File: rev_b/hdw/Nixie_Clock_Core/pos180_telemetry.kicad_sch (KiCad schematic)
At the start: 27 parts, among them Q701 BSS192PH6327FTSA1, U701 OPA333xxDCK, U704 OPA333xxDCK, U705 OPA333xxDCK

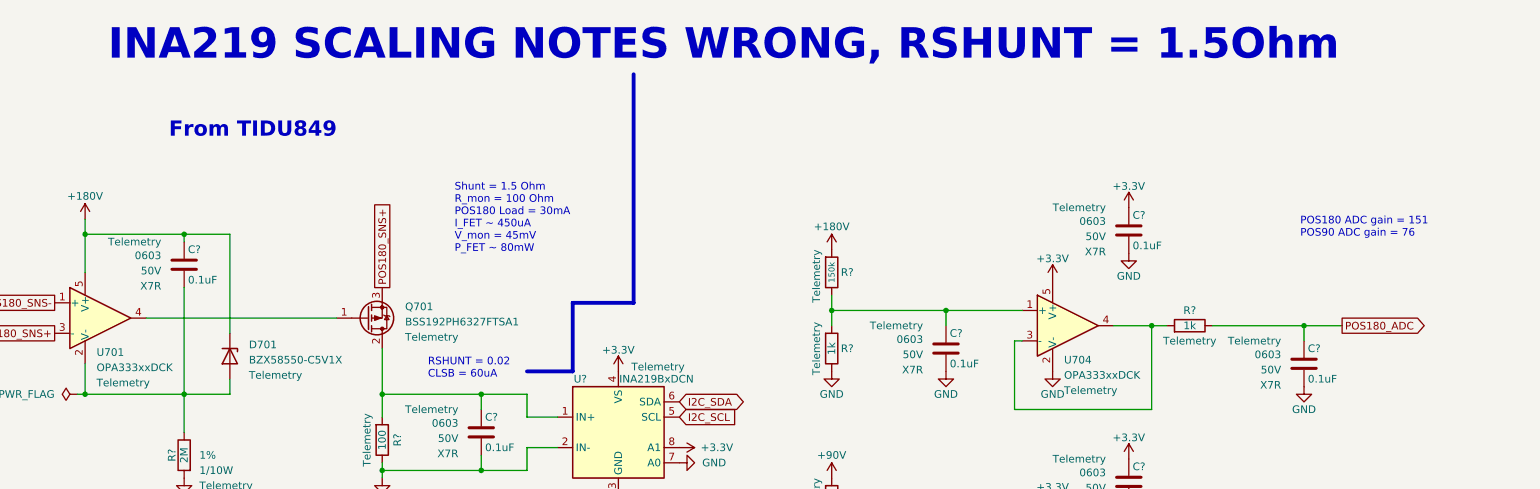
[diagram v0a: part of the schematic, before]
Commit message: added BOM
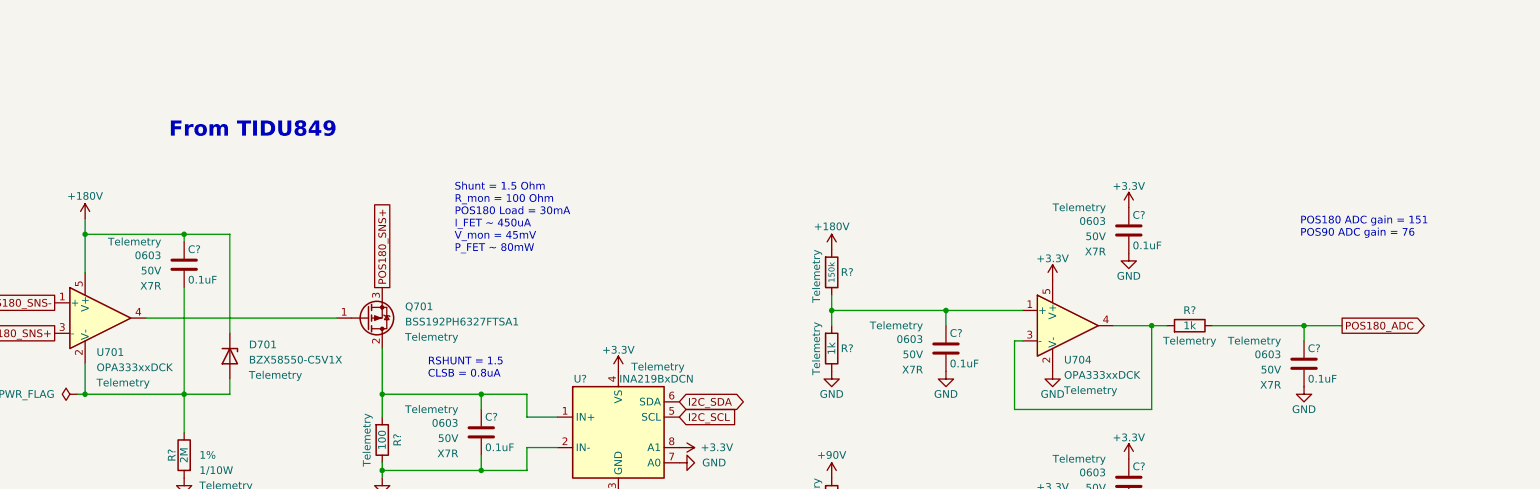
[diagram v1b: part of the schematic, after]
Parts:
- R?: Digi-Key PN (none) -> 541-CRCW0603150KFKTACT-ND
- R? (x4): Digi-Key PN (none) -> 541-1.00KHCT-ND
- R?: Digi-Key PN (none) -> 541-5552-1-ND
- R?: Digi-Key PN (none) -> 541-3951-1-ND
- R?: Digi-Key PN (none) -> 541-5333-1-ND
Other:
- note added: "RSHUNT = 1.5 CLSB = 0.8uA"
- note removed: "INA219 SCALING NOTES WRONG, RSHUNT = 1.5Ohm"
- note removed: "RSHUNT = 0.02 CLSB = 60uA"
- title: (none) -> Nixie Clock Redux Core Board
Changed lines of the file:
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@@
   (paper "A")
   (title_block
-    (date "2023-05-12")
-    (rev "PRELIM")
+    (title "Nixie Clock Redux Core Board")
+    (date "2023-07-30")
+    (rev "B")
     (company "Drew Maatman")
   )
@@
     (stroke (width 0) (type default))
   )
-  (polyline (pts (xy 128.27 34.29) (xy 128.27 72.39))
-    (stroke (width 0.635) (type default) (color 255 0 0 1))
-  )
   (wire (pts (xy 208.28 114.3) (xy 214.63 114.3))
     (stroke (width 0) (type default))
@@
     (stroke (width 0) (type default))
   )
-  (polyline (pts (xy 118.11 72.39) (xy 128.27 72.39))
-    (stroke (width 0.635) (type default) (color 255 0 0 1))
-  )
   (wire (pts (xy 86.36 100.33) (xy 86.36 101.6))
     (stroke (width 0) (type default))
@@
     (stroke (width 0) (type default))
   )
-  (polyline (pts (xy 110.49 83.82) (xy 118.11 83.82))
-    (stroke (width 0.635) (type default) (color 255 0 0 1))
-  )
   (wire (pts (xy 86.36 100.33) (xy 102.87 100.33))
     (stroke (width 0) (type default))
@@
     (stroke (width 0) (type default))
   )
-  (polyline (pts (xy 118.11 83.82) (xy 118.11 72.39))
-    (stroke (width 0.635) (type default) (color 255 0 0 1))
-  )
   (wire (pts (xy 224.79 76.2) (xy 240.03 76.2))
     (stroke (width 0) (type default))
@@
     (effects (font (size 1.27 1.27)) (justify left bottom))
   )
-  (text "RSHUNT = 0.02\nCLSB = 60uA" (at 93.98 85.09 0)
+  (text "RSHUNT = 1.5\nCLSB = 0.8uA" (at 93.98 85.09 0)
     (effects (font (size 1.27 1.27)) (justify left bottom))
   )
@@
     (effects (font (size 1.27 1.27)) (justify left bottom))
   )
-  (text "INA219 SCALING NOTES WRONG, RSHUNT = 1.5Ohm" (at 40.64 32.385 0)
-    (effects (font (face "Courier New") (size 5.08 5.08) (thickness 0.254) bold (color 255 37 56 1)) (justify left bottom))
-  )
-  (global_label "I2C_SDA" (shape bidirectional) (at 135.89 88.9 0)
+  (global_label "I2C_SDA" (shape bidirectional) (at 135.89 88.9 0) (fields_autoplaced)
     (effects (font (size 1.27 1.27)) (justify left))
-    (property "Intersheetrefs" "${INTERSHEET_REFS}" (at 135.89 88.9 0)
-      (effects (font (size 1.27 1.27)) hide)
+    (property "Intersheetrefs" "${INTERSHEET_REFS}" (at 147.5271 88.9 0)
+      (effects (font (size 1.27 1.27)) (justify left))
     )
   )
-  (global_label "I2C_SDA" (shape bidirectional) (at 57.15 156.21 0)
+  (global_label "I2C_SDA" (shape bidirectional) (at 57.15 156.21 0) (fields_autoplaced)
     (effects (font (size 1.27 1.27)) (justify left))
-    (property "Intersheetrefs" "${INTERSHEET_REFS}" (at 57.15 156.21 0)
-      (effects (font (size 1.27 1.27)) hide)
+    (property "Intersheetrefs" "${INTERSHEET_REFS}" (at 68.7871 156.21 0)
+      (effects (font (size 1.27 1.27)) (justify left))
     )
   )
-  (global_label "I2C_SCL" (shape input) (at 57.15 158.75 0)
+  (global_label "I2C_SCL" (shape input) (at 57.15 158.75 0) (fields_autoplaced)
     (effects (font (size 1.27 1.27)) (justify left))
-    (property "Intersheetrefs" "${INTERSHEET_REFS}" (at 57.15 158.75 0)
-      (effects (font (size 1.27 1.27)) hide)
+    (property "Intersheetrefs" "${INTERSHEET_REFS}" (at 67.6153 158.75 0)
+      (effects (font (size 1.27 1.27)) (justify left))
     )
   )
-  (global_label "POS180_SNS+" (shape passive) (at 86.36 69.85 90)
+  (global_label "POS180_SNS+" (shape passive) (at 86.36 69.85 90) (fields_autoplaced)
     (effects (font (size 1.27 1.27)) (justify left))
-    (property "Intersheetrefs" "${INTERSHEET_REFS}" (at 86.36 69.85 0)
-      (effects (font (size 1.27 1.27)) hide)
+    (property "Intersheetrefs" "${INTERSHEET_REFS}" (at 86.36 54.3275 90)
+      (effects (font (size 1.27 1.27)) (justify left))
     )
   )
-  (global_label "POS180_SNS+" (shape passive) (at 31.75 77.47 180)
+  (global_label "POS180_SNS+" (shape passive) (at 31.75 77.47 180) (fields_autoplaced)
     (effects (font (size 1.27 1.27)) (justify right))
-    (property "Intersheetrefs" "${INTERSHEET_REFS}" (at 31.75 77.47 0)
-      (effects (font (size 1.27 1.27)) hide)
+    (property "Intersheetrefs" "${INTERSHEET_REFS}" (at 16.2275 77.47 0)
+      (effects (font (size 1.27 1.27)) (justify right))
     )
   )
@@
     (effects (font (size 1.27 1.27)) (justify left))
     (property "Intersheetrefs" "${INTERSHEET_REFS}" (at 260.111 114.3 0)
-      (effects (font (size 1.27 1.27)) (justify left) hide)
+      (effects (font (size 1.27 1.27)) (justify left))
     )
   )
@@
     (effects (font (size 1.27 1.27)) (justify left))
     (property "Intersheetrefs" "${INTERSHEET_REFS}" (at 261.3205 76.2 0)
-      (effects (font (size 1.27 1.27)) (justify left) hide)
+      (effects (font (size 1.27 1.27)) (justify left))
     )
   )
-  (global_label "POS180_SNS-" (shape passive) (at 31.75 72.39 180)
+  (global_label "POS180_SNS-" (shape passive) (at 31.75 72.39 180) (fields_autoplaced)
     (effects (font (size 1.27 1.27)) (justify right))
-    (property "Intersheetrefs" "${INTERSHEET_REFS}" (at 31.75 72.39 0)
-      (effects (font (size 1.27 1.27)) hide)
+    (property "Intersheetrefs" "${INTERSHEET_REFS}" (at 16.2275 72.39 0)
+      (effects (font (size 1.27 1.27)) (justify right))
     )
   )
-  (global_label "I2C_SCL" (shape input) (at 135.89 91.44 0)
+  (global_label "I2C_SCL" (shape input) (at 135.89 91.44 0) (fields_autoplaced)
     (effects (font (size 1.27 1.27)) (justify left))
-    (property "Intersheetrefs" "${INTERSHEET_REFS}" (at 135.89 91.44 0)
-      (effects (font (size 1.27 1.27)) hide)
+    (property "Intersheetrefs" "${INTERSHEET_REFS}" (at 146.3553 91.44 0)
+      (effects (font (size 1.27 1.27)) (justify left))
     )
   )
@@
       (effects (font (size 1.27 1.27)) (justify left) hide)
     )
-    (property "Digi-Key PN" "" (at 153.67 57.15 0)
+    (property "Digi-Key PN" "541-CRCW0603150KFKTACT-ND" (at 153.67 57.15 0)
       (effects (font (size 1.524 1.524)) hide)
     )
@@
       (effects (font (size 1.27 1.27)) (justify left) hide)
     )
-    (property "Digi-Key PN" "" (at 210.82 83.82 0)
+    (property "Digi-Key PN" "541-1.00KHCT-ND" (at 210.82 83.82 0)
       (effects (font (size 1.524 1.524)) hide)
     )
@@
       (effects (font (size 1.27 1.27)) (justify left) hide)
     )
-    (property "Digi-Key PN" "" (at 153.67 95.25 0)
+    (property "Digi-Key PN" "541-5552-1-ND" (at 153.67 95.25 0)
       (effects (font (size 1.524 1.524)) hide)
     )
@@
       (effects (font (size 1.27 1.27)) hide)
     )
-    (property "Digi-Key PN" "" (at 86.36 95.25 0)
+    (property "Digi-Key PN" "541-3951-1-ND" (at 86.36 95.25 0)
       (effects (font (size 1.27 1.27)) hide)
     )
@@
       (effects (font (size 1.27 1.27)) (justify left) hide)
     )
-    (property "Digi-Key PN" "" (at 153.67 69.85 0)
+    (property "Digi-Key PN" "541-1.00KHCT-ND" (at 153.67 69.85 0)
       (effects (font (size 1.524 1.524)) hide)
     )
@@
       (effects (font (size 1.27 1.27)) hide)
     )
+    (property "Digi-Key PN" "541-5333-1-ND" (at 53.34 97.79 0)
+      (effects (font (size 1.27 1.27)) hide)
+    )
     (pin "1")
     (pin "2")
@@
       (effects (font (size 1.27 1.27)) (justify left) hide)
     )
-    (property "Digi-Key PN" "" (at 153.67 107.95 0)
+    (property "Digi-Key PN" "541-1.00KHCT-ND" (at 153.67 107.95 0)
       (effects (font (size 1.524 1.524)) hide)
     )
@@
       (effects (font (size 1.27 1.27)) (justify left) hide)
     )
-    (property "Digi-Key PN" "" (at 210.82 121.92 0)
+    (property "Digi-Key PN" "541-1.00KHCT-ND" (at 210.82 121.92 0)
       (effects (font (size 1.524 1.524)) hide)
     )
